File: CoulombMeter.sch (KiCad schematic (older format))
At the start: 19 parts, among them IC1 ATMEGA328P-P, P1 CONN_02X03, P10 CONN_01X03, P2 CONN_01X10, P3 CONN_01X06, P4 USB_OTG, P5 OUTPUT, P6 INPUT, P7 CONN_01X10, P8 OUTPUT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

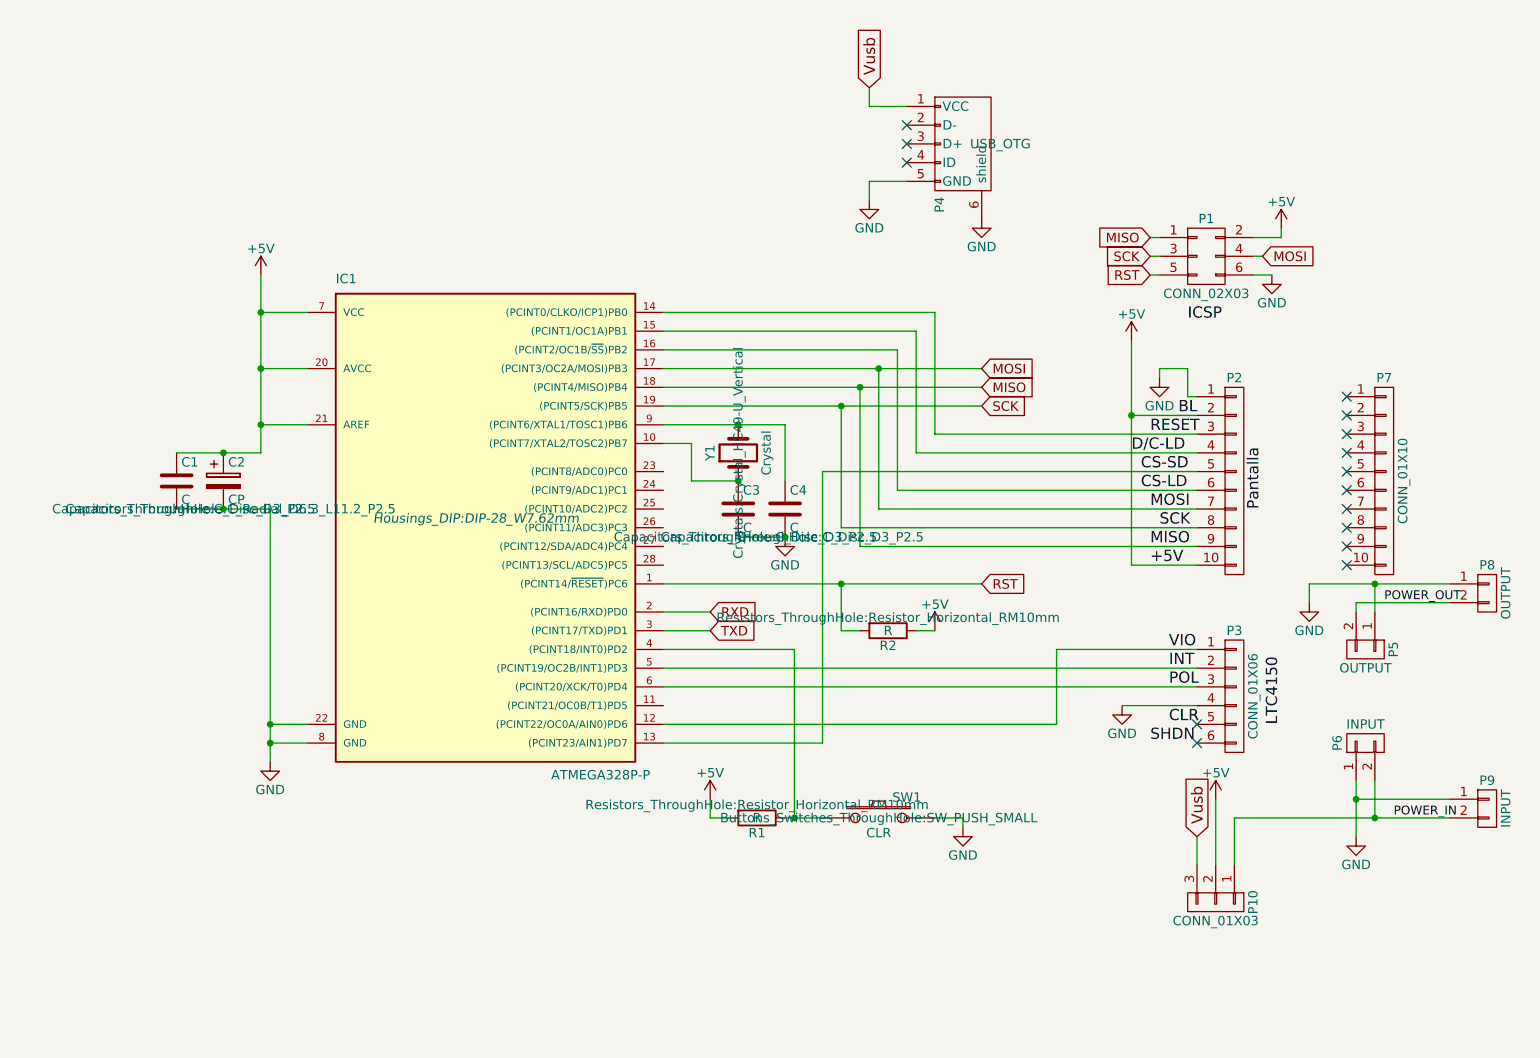
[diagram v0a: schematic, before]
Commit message: Fix display socket orientation
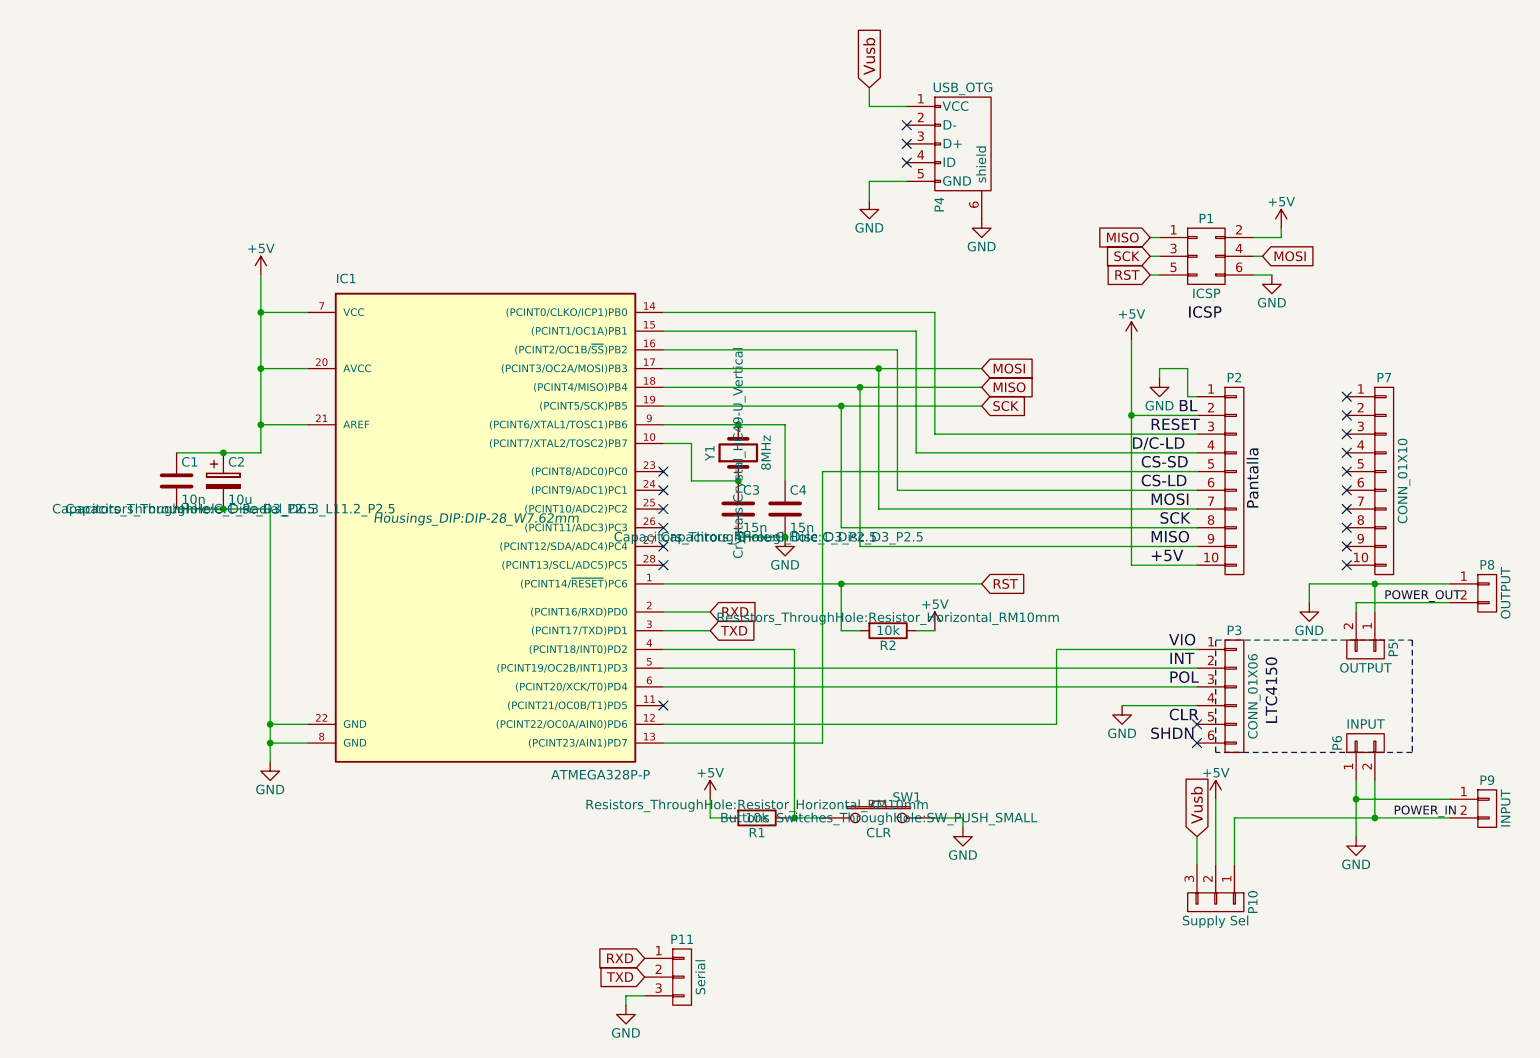
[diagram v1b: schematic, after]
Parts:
- added P11: Serial, Pin_Headers:Pin_Header_Straight_1x03, symbol CONN_01X03
- C1: value C -> 10n
- C2: value CP -> 10u
- C3, C4: value C -> 15n
- P1: value CONN_02X03 -> ICSP
- P10: value CONN_01X03 -> Supply Sel
- R1, R2: value R -> 10k
- Y1: value Crystal -> 8MHz
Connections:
- net GND: now also P11.3 (P3)
- net RXD: now also P11.1 (P1)
- net TXD: now also P11.2 (P2)
- no-connect marks 15 -> 22
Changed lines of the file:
@@
 LIBS:contrib
 LIBS:valves
+LIBS:w_connectors
 LIBS:CoulombMeter-cache
 EELAYER 25 0
@@
 P 8350 2550
 F 0 "P1" H 8350 2750 50  0000 C CNN
-F 1 "CONN_02X03" H 8350 2350 50  0000 C CNN
+F 1 "ICSP" H 8350 2350 50  0000 C CNN
 F 2 "Pin_Headers:Pin_Header_Angled_2x03" H 8350 1350 50  0001 C CNN
 F 3 "" H 8350 1350 50  0000 C CNN
@@
 P 5950 5550
 F 0 "R1" V 6030 5550 50  0000 C CNN
-F 1 "R" V 5950 5550 50  0000 C CNN
+F 1 "10k" V 5950 5550 50  0000 C CNN
 F 2 "Resistors_ThroughHole:Resistor_Horizontal_RM10mm" V 5880 5550 50  0000 C CNN
 F 3 "" H 5950 5550 50  0000 C CNN
@@
 P 3100 3750
 F 0 "C2" H 3125 3850 50  0000 L CNN
-F 1 "CP" H 3125 3650 50  0000 L CNN
+F 1 "10u" H 3125 3650 50  0000 L CNN
 F 2 "Capacitors_ThroughHole:C_Radial_D6.3_L11.2_P2.5" H 3138 3600 50  0000 C CNN
 F 3 "" H 3100 3750 50  0000 C CNN
@@
 P 2850 3750
 F 0 "C1" H 2875 3850 50  0000 L CNN
-F 1 "C" H 2875 3650 50  0000 L CNN
+F 1 "10n" H 2875 3650 50  0000 L CNN
 F 2 "Capacitors_ThroughHole:C_Disc_D3_P2.5" H 2888 3600 50  0000 C CNN
 F 3 "" H 2850 3750 50  0000 C CNN
@@
 P 5850 3600
 F 0 "Y1" H 5850 3750 50  0000 C CNN
-F 1 "Crystal" H 5850 3450 50  0000 C CNN
+F 1 "8MHz" H 5850 3450 50  0000 C CNN
 F 2 "Crystals:Crystal_HC49-U_Vertical" H 5850 3600 50  0000 C CNN
 F 3 "" H 5850 3600 50  0000 C CNN
@@
 P 5850 3900
 F 0 "C3" H 5875 4000 50  0000 L CNN
-F 1 "C" H 5875 3800 50  0000 L CNN
+F 1 "15n" H 5875 3800 50  0000 L CNN
 F 2 "Capacitors_ThroughHole:C_Disc_D3_P2.5" H 5888 3750 50  0000 C CNN
 F 3 "" H 5850 3900 50  0000 C CNN
@@
 P 6100 3900
 F 0 "C4" H 6125 4000 50  0000 L CNN
-F 1 "C" H 6125 3800 50  0000 L CNN
+F 1 "15n" H 6125 3800 50  0000 L CNN
 F 2 "Capacitors_ThroughHole:C_Disc_D3_P2.5" H 6138 3750 50  0000 C CNN
 F 3 "" H 6100 3900 50  0000 C CNN
@@
 P 7050 1950
 F 0 "P4" H 7375 1825 50  0000 C CNN
-F 1 "USB_OTG" V 7050 2150 50  0000 C CNN
+F 1 "USB_OTG" V 6750 1950 50  0000 C CNN
 F 2 "Connect:USB_Micro-B" V 7000 1850 50  0001 C CNN
 F 3 "" V 7000 1850 50  0000 C CNN
@@
 P 6650 4550
 F 0 "R2" V 6730 4550 50  0000 C CNN
-F 1 "R" V 6650 4550 50  0000 C CNN
+F 1 "10k" V 6650 4550 50  0000 C CNN
 F 2 "Resistors_ThroughHole:Resistor_Horizontal_RM10mm" V 6580 4550 50  0000 C CNN
 F 3 "" H 6650 4550 50  0000 C CNN
@@
 P 8400 6000
 F 0 "P10" H 8400 6200 50  0000 C CNN
-F 1 "CONN_01X03" V 8500 6000 50  0000 C CNN
+F 1 "Supply Sel" V 8500 6000 50  0000 C CNN
 F 2 "Pin_Headers:Pin_Header_Straight_1x03" H 8400 6000 50  0001 C CNN
 F 3 "" H 8400 6000 50  0000 C CNN
@@
 Text Label 9300 4400 0    47   ~ 0
 POWER_OUT
+Wire Notes Line
+	8400 4600 9450 4600
+Wire Notes Line
+	9450 4600 9450 5200
+Wire Notes Line
+	9450 5200 8400 5200
+Wire Notes Line
+	8400 5200 8400 4600
+$Comp
+L CONN_01X03 P11
+U 1 1 5A397CFE
+P 5550 6400
+F 0 "P11" H 5550 6600 50  0000 C CNN
+F 1 "Serial" V 5650 6400 50  0000 C CNN
+F 2 "Pin_Headers:Pin_Header_Straight_1x03" H 5550 6400 50  0001 C CNN
+F 3 "" H 5550 6400 50  0000 C CNN
+	1    5550 6400
+	1    0    0    -1
+$EndComp
+Text GLabel 5350 6400 0    51   Input ~ 0
+TXD
+Text GLabel 5350 6300 0    51   Input ~ 0
+RXD
+$Comp
+L GND #PWR017
+U 1 1 5A398451
+P 5250 6550
+F 0 "#PWR017" H 5250 6300 50  0001 C CNN
+F 1 "GND" H 5250 6400 50  0000 C CNN
+F 2 "" H 5250 6550 50  0000 C CNN
+F 3 "" H 5250 6550 50  0000 C CNN
+	1    5250 6550
+	1    0    0    -1
+$EndComp
+Wire Wire Line
+	5350 6500 5250 6500
+Wire Wire Line
+	5250 6500 5250 6550
+NoConn ~ 5450 3700
+NoConn ~ 5450 3800
+NoConn ~ 5450 3900
+NoConn ~ 5450 4000
+NoConn ~ 5450 4100
+NoConn ~ 5450 4200
+NoConn ~ 5450 4950
 $EndSCHEMATC

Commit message: Relocate display
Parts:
- added P12: CURRENT, Pin_Headers:Pin_Header_Angled_1x02_Pitch2.54mm, symbol CONN_01X02
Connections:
- net POWER_IN: now also P12.2 (P2)
- net POWER_OUT: now also P12.1 (P1)
- net SHDN: now also IC1.11 ((PCINT21/OC0B/T1)PD5), P3.6 (P6)
- no-connect marks 22 -> 20
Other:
- moved on the sheet: P9
